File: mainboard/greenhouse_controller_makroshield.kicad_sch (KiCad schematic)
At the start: 39 parts

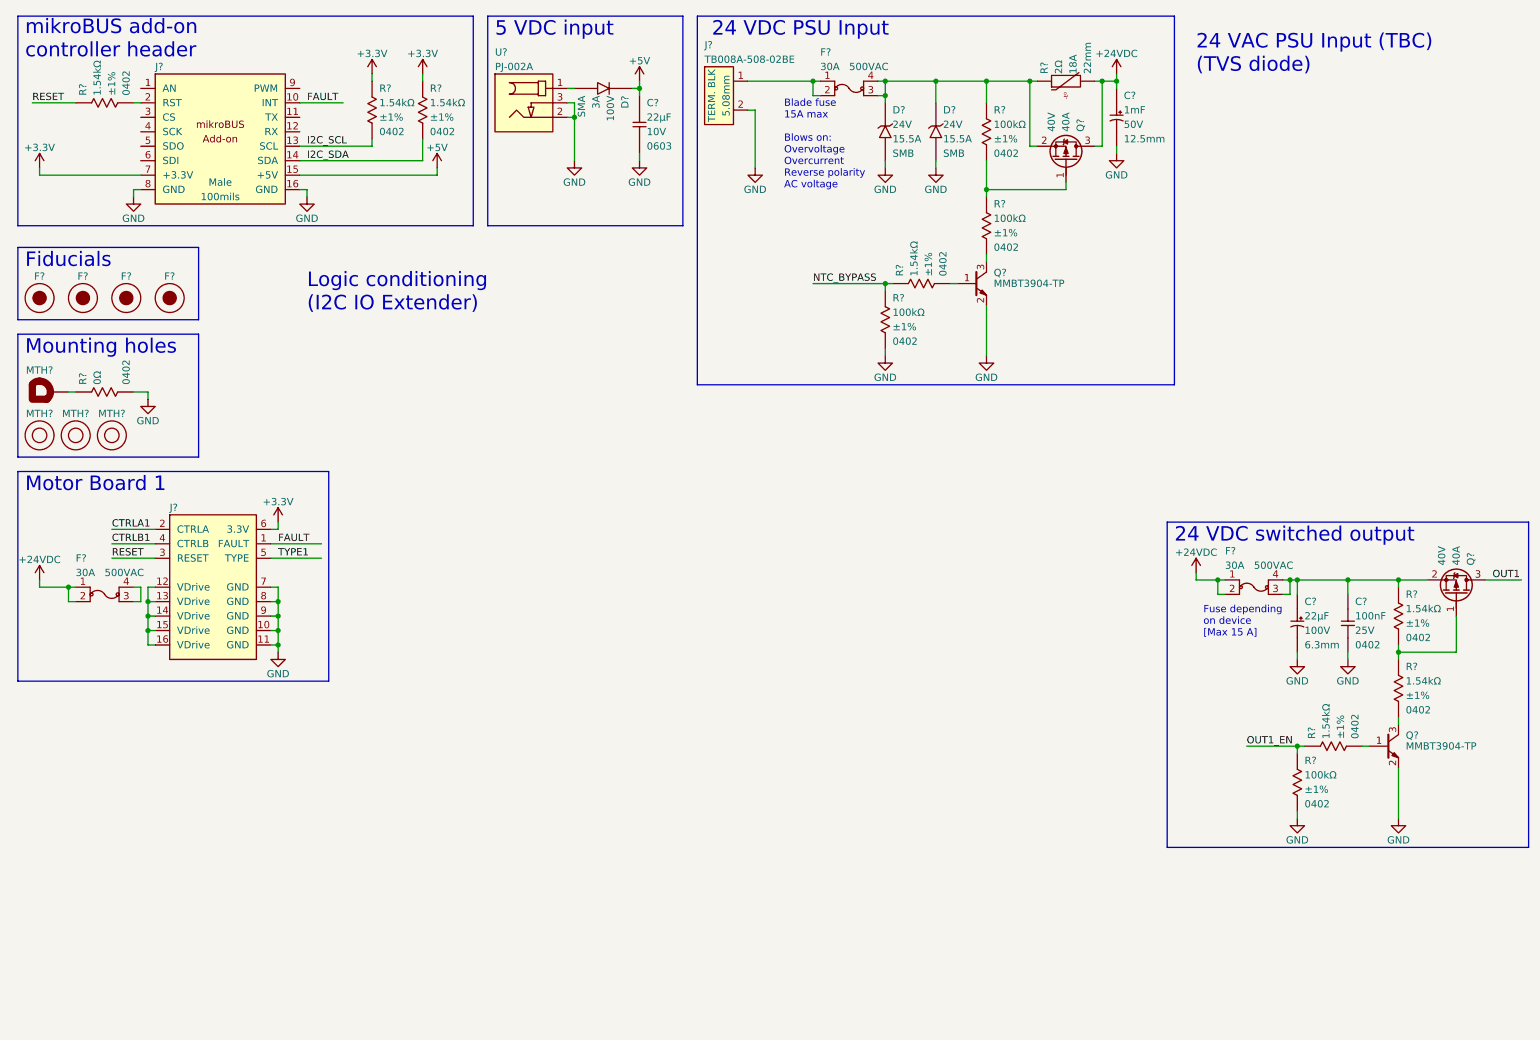
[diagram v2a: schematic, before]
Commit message: Add IO expanders, add simple PMOS switch, add 5V TVS,
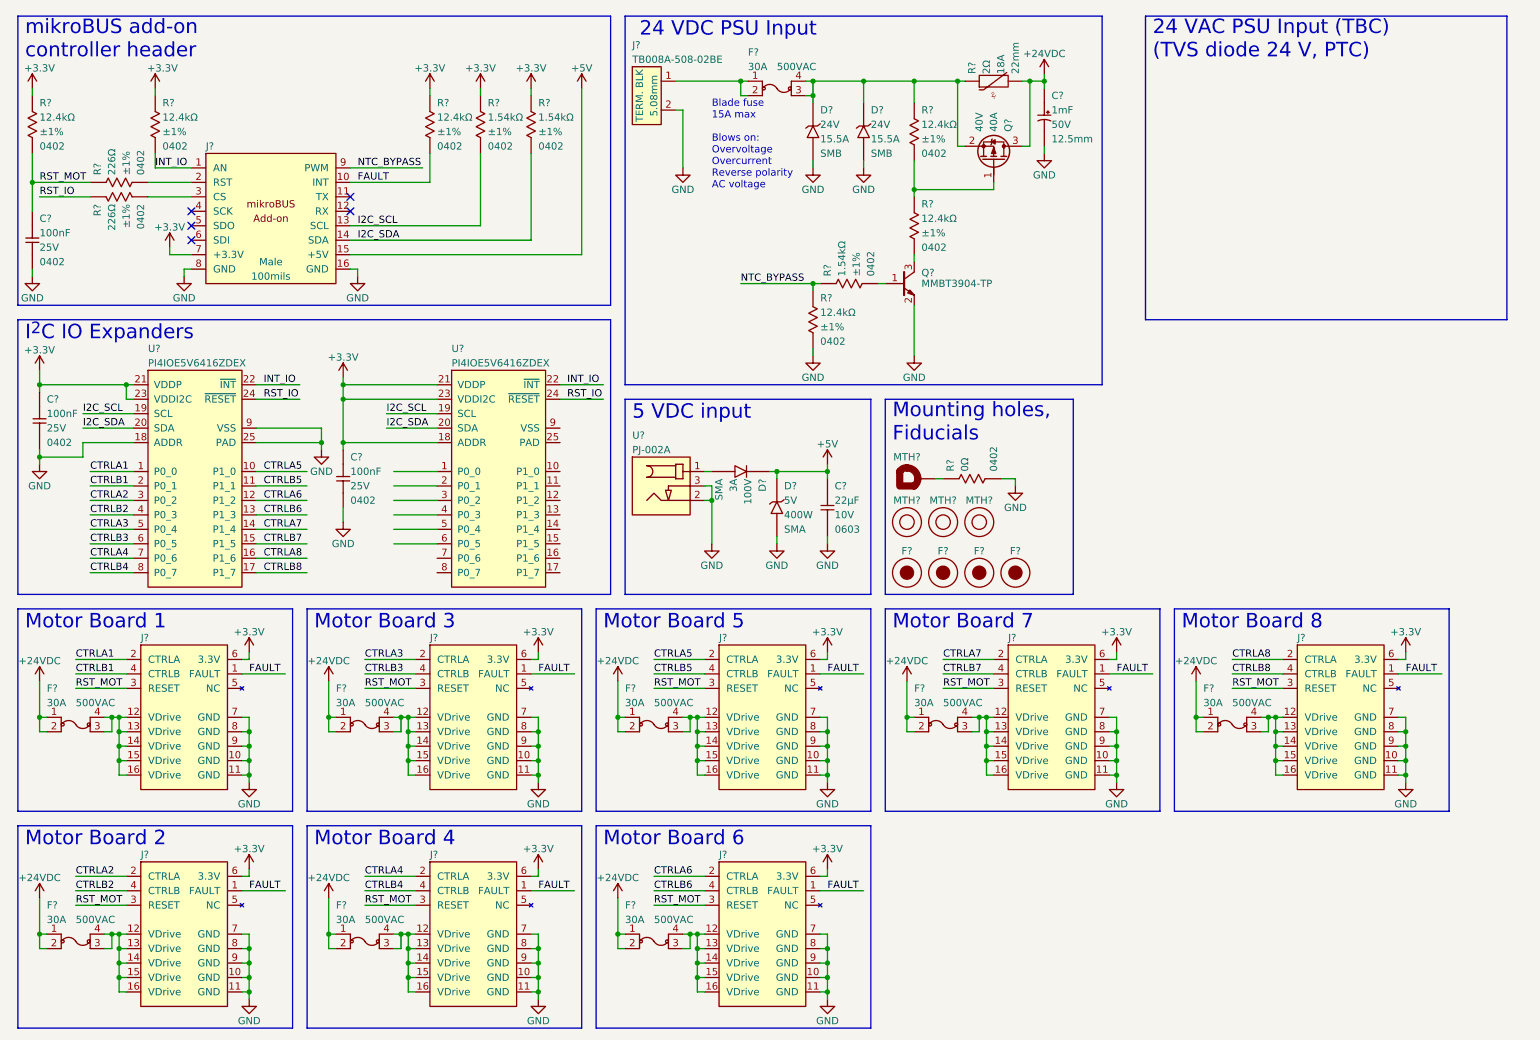
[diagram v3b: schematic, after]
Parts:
- removed C?: CAP_CER_100NF_25V_0402, connaxio-capacitors:CAP_CER_0402_1005M, symbol connaxio-capacitors:CAP_CER_100NF_25V_0402
- removed C?: CAP_AE_22UF_100V_TH_6.3MM, connaxio-capacitors:CAP_AE_RAD_D6.3_H12.5_P2.5, symbol connaxio-capacitors:CAP_AE_22UF_100V_TH_6.3MM
- removed F?: FUS_BLADE_3522, connaxio-connectors:FUS_BLADE_3522, symbol connaxio-connectors:FUS_BLADE_3522
- removed Q?: TRX_PMOS_AOD4189, connaxio-sop:TO-252-3, symbol connaxio-transistors:TRX_PMOS_AOD4189
- removed Q?: TRX_NPN_MMBT3904-TP, connaxio-sop:SOT-23-3, symbol connaxio-transistors:TRX_NPN_MMBT3904-TP
- removed R? (x4): RES_100KΩ_1%_0402, connaxio-resistors:RES_0402_1005M, symbol connaxio-resistors:RES_100KΩ_1%_0402
- removed R? (x4): RES_1.54KΩ_1%_0402, connaxio-resistors:RES_0402_1005M, symbol connaxio-resistors:RES_1.54KΩ_1%_0402
- added C? (x3): CAP_CER_100NF_25V_0402, connaxio-capacitors:CAP_CER_0402_1005M, symbol connaxio-capacitors:CAP_CER_100NF_25V_0402
- added D?: DIO_TVS_5V_UNI_SMA, connaxio-diodes:DO-214AC_SMA, symbol connaxio-diodes:DIO_TVS_5V_UNI_SMA
- added F? (x7): FUS_BLADE_3522, connaxio-connectors:FUS_BLADE_3522, symbol connaxio-connectors:FUS_BLADE_3522
- added J? (x7): CON_CONNAXIO_MOTOR_DRIVER, connaxio-connectors:CON_HDR_100MILS_F_TH_2X8, symbol connaxio-connectors:CON_CONNAXIO_MOTOR_DRIVER
- added R? (x6): RES_12.4KΩ_1%_0402, connaxio-resistors:RES_0402_1005M, symbol connaxio-resistors:RES_12.4KΩ_1%_0402
- added R? (x2): RES_226Ω_1%_0402, connaxio-resistors:RES_0402_1005M, symbol connaxio-resistors:RES_226Ω_1%_0402
- added U? (x2): IO_EXP_PI4IOE5V6416ZDEX, connaxio-fp:QFN-24_4x4_P0.5_EP2.7X2.7, symbol connaxio-ic:IO_EXP_PI4IOE5V6416ZDEX
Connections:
- net +24VDC: now also F?.1, F?.1, F?.1, F?.1, F?.1, F?.1, F?.1, F?.2, F?.2, F?.2, F?.2, F?.2, F?.2, F?.2
- net +3.3V: now also C?.1, C?.1, J?.6 (3.3V), J?.6 (3.3V), J?.6 (3.3V), J?.6 (3.3V), J?.6 (3.3V), J?.6 (3.3V), J?.6 (3.3V), R?.1, R?.1, R?.1, U?.18 (ADDR), U?.21 (VDDP), U?.21 (VDDP), U?.23 (VDDI2C), U?.23 (VDDI2C)
- net +5V: now also D?.1 (K)
- net CTRLA1: now also U?.1 (P0_0)
- net CTRLB1: now also U?.2 (P0_1)
- net FAULT: now also J?.1 (FAULT), J?.1 (FAULT), J?.1 (FAULT), J?.1 (FAULT), J?.1 (FAULT), J?.1 (FAULT), J?.1 (FAULT), R?.2
- net GND: now also C?.2, C?.2, C?.2, D?.2 (A), J?.10 (GND), J?.10 (GND), J?.10 (GND), J?.10 (GND), J?.10 (GND), J?.10 (GND), J?.10 (GND), J?.11 (GND), J?.11 (GND), J?.11 (GND), J?.11 (GND), J?.11 (GND), J?.11 (GND), J?.11 (GND), J?.7 (GND), J?.7 (GND), J?.7 (GND), J?.7 (GND), J?.7 (GND), J?.7 (GND), J?.7 (GND), J?.8 (GND), J?.8 (GND), J?.8 (GND), J?.8 (GND), J?.8 (GND), J?.8 (GND), J?.8 (GND), J?.9 (GND), J?.9 (GND), J?.9 (GND), J?.9 (GND), J?.9 (GND), J?.9 (GND), J?.9 (GND), R?.2, U?.18 (ADDR), U?.25 (PAD), U?.9 (VSS)
- net I2C_SCL: now also U?.19 (SCL), U?.19 (SCL)
- net I2C_SDA: now also U?.20 (SDA), U?.20 (SDA)
- net NTC_BYPASS: now also J?.9 (PWM), R?.1
- net at D?.1 (K), D?.1 (K), F?.3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: now also R?.1
- net at Q?.1 (G): now also R?.1, R?.2
- net at Q?.3 (C): now also R?.2
- net at J?.2 (RST): now also R?.2
- net at F?.3, F?.4: now also J?.12 (VDrive), J?.13 (VDrive), J?.14 (VDrive), J?.15 (VDrive), J?.16 (VDrive)
- net INT_IO: now reaches J?.1 (AN)
- net INT_IO: now also R?.2, U?.22 (~{INT}), U?.22 (~{INT})
- net at J?.3 (CS): now also R?.2
- net RESET renamed RST_MOT
- net RST_MOT: now also C?.1, J?.3 (RESET), J?.3 (RESET), J?.3 (RESET), J?.3 (RESET), J?.3 (RESET), J?.3 (RESET), J?.3 (RESET), R?.1, R?.2
- net TYPE1: no longer names the net of J?.5 (NC)
- new net: F?.3, F?.4, J?.12 (VDrive), J?.13 (VDrive), J?.14 (VDrive), J?.15 (VDrive), J?.16 (VDrive) (x7)
- new net CTRLA2: J?.2 (CTRLA), U?.3 (P0_2)
- new net CTRLA3: J?.2 (CTRLA), U?.5 (P0_4)
- new net CTRLA4: J?.2 (CTRLA), U?.7 (P0_6)
- new net CTRLA5: J?.2 (CTRLA), U?.10 (P1_0)
- new net CTRLA6: J?.2 (CTRLA), U?.12 (P1_2)
- new net CTRLA7: J?.2 (CTRLA), U?.14 (P1_4)
- new net CTRLA8: J?.2 (CTRLA), U?.16 (P1_6)
- new net CTRLB2: J?.4 (CTRLB), U?.4 (P0_3)
- new net CTRLB3: J?.4 (CTRLB), U?.6 (P0_5)
- new net CTRLB4: J?.4 (CTRLB), U?.8 (P0_7)
- new net CTRLB5: J?.4 (CTRLB), U?.11 (P1_1)
- new net CTRLB6: J?.4 (CTRLB), U?.13 (P1_3)
- new net CTRLB7: J?.4 (CTRLB), U?.15 (P1_5)
- new net CTRLB8: J?.4 (CTRLB), U?.17 (P1_7)
- new net RST_IO: R?.1, U?.24 (~{RESET}), U?.24 (~{RESET})
- no-connect marks 0 -> 5
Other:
- note added: "24 VAC PSU Input (TBC) (TVS diode 24 V, PTC)"
- note added: "I^{2}C IO Expanders"
- note added: "Motor Board 2"
- note added: "Motor Board 3"
- note added: "Motor Board 4"
- note added: "Motor Board 5"
- note added: "Motor Board 6"
- note added: "Motor Board 7"
- note added: "Motor Board 8"
- note added: "Mounting holes, Fiducials"
- note removed: "24 VAC PSU Input (TBC) (TVS diode)"
- note removed: "24 VDC switched output"
- note removed: "Fiducials"
- note removed: "Fuse depending on device [Max 15 A]"
- note removed: "Logic conditioning (I2C IO Extender)"
- note removed: "Mounting holes"
- moved on the sheet: C?, D?, F?, J?, MTH?, Q?, R?, U?

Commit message: Add motor driver page and I2C proteciton adapter, current & temp sensor
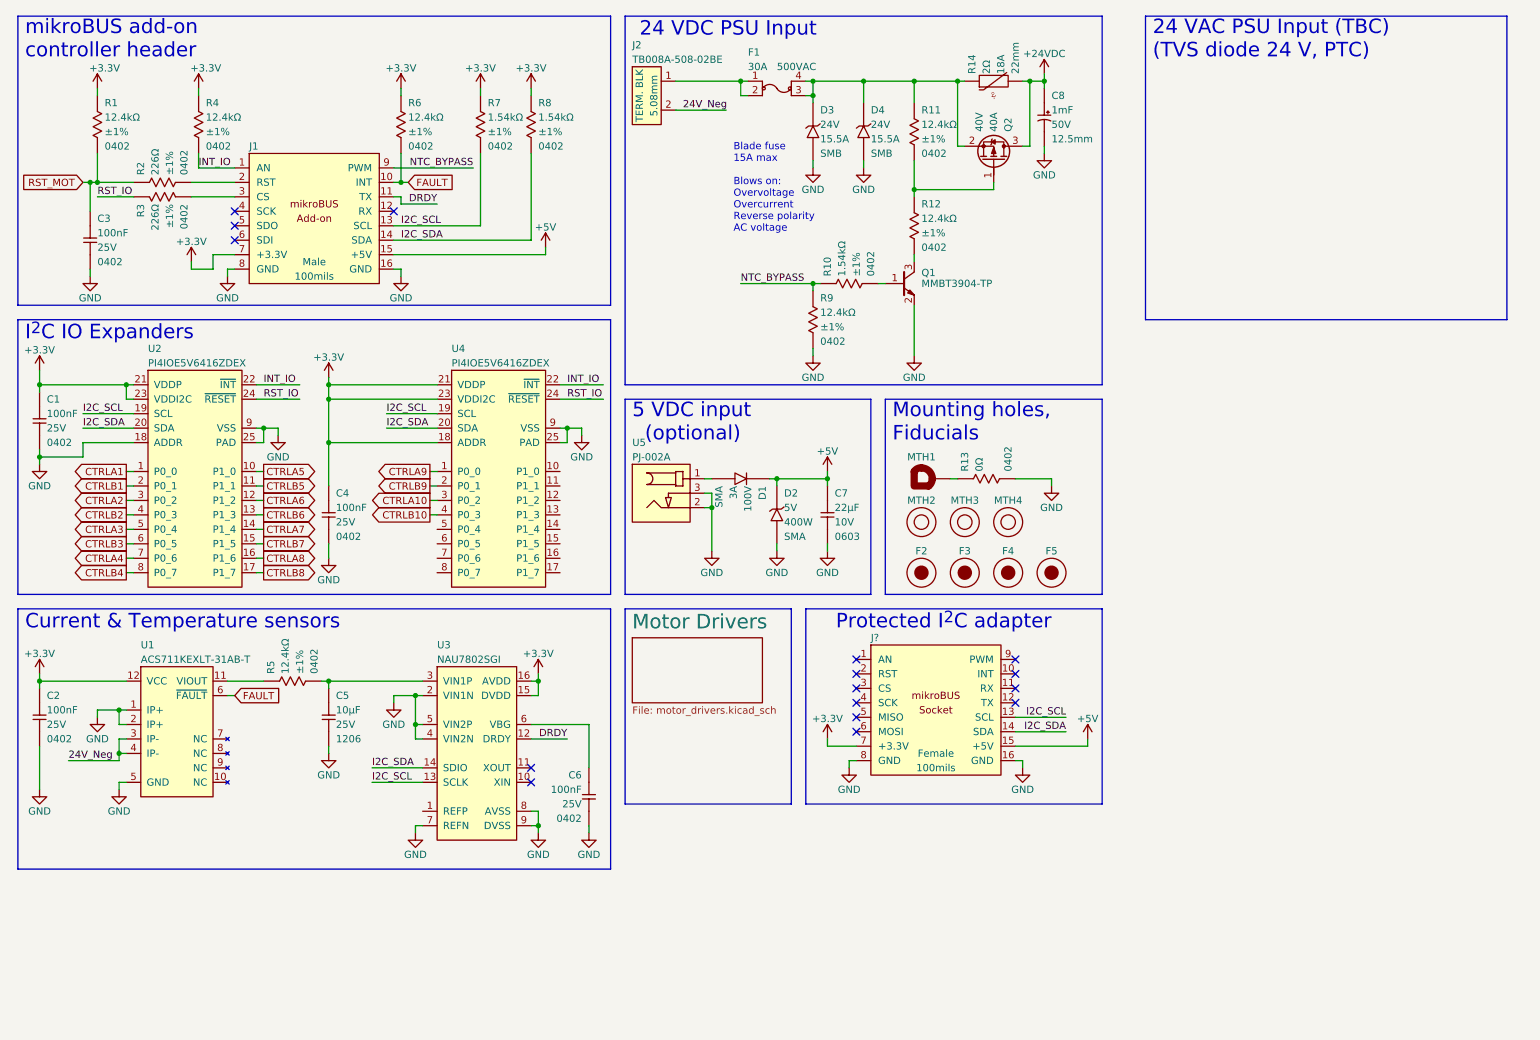
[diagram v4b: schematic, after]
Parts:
- removed F? (x8): FUS_BLADE_3522, connaxio-connectors:FUS_BLADE_3522, symbol connaxio-connectors:FUS_BLADE_3522
- removed J? (x8): CON_CONNAXIO_MOTOR_DRIVER, connaxio-connectors:CON_HDR_100MILS_F_TH_2X8, symbol connaxio-connectors:CON_CONNAXIO_MOTOR_DRIVER
- added C2, C6: CAP_CER_100NF_25V_0402, connaxio-capacitors:CAP_CER_0402_1005M, symbol connaxio-capacitors:CAP_CER_100NF_25V_0402
- added C5: CAP_CER_10UF_25V_1206, connaxio-capacitors:CAP_CER_1206_3216M, symbol connaxio-capacitors:CAP_CER_10UF_25V_1206
- added J?: CON_HDR_MIKROBUS_SOCKET_TH, connaxio-connectors:CON_HDR_MIKROBUS_SOCKET_TH, symbol connaxio-connectors:CON_HDR_MIKROBUS_SOCKET_TH
- added R5: RES_12.4KΩ_1%_0402, connaxio-resistors:RES_0402_1005M, symbol connaxio-resistors:RES_12.4KΩ_1%_0402
- added U1: SUN_CUR_ACS711KEXLT-31AB-T, connaxio-fp:QFN-12_CUR_SEN_ACS7, symbol connaxio-ic:SUN_CUR_ACS711KEXLT-31AB-T
- added U3: ADC_NAU7802SGI, connaxio-sop:SOIC-16_3.9X9.9_P1.27, symbol connaxio-ic:ADC_NAU7802SGI
- gave numbers to parts that had none: 38
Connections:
- net +3.3V: now also C2.1, J?.7 (+3.3V), U1.12 (VCC), U3.15 (DVDD), U3.16 (AVDD)
- net +5V: now also J?.15 (+5V)
- net FAULT: now also U1.6 (~{FAULT})
- net GND: now also U4.25 (PAD), U4.9 (VSS), C2.2, C5.2, C6.2, J?.16 (GND), J?.8 (GND), U1.1 (IP+), U1.2 (IP+), U1.5 (GND), U3.2 (VIN1N), U3.4 (VIN2N), U3.5 (VIN2P), U3.7 (REFN), U3.8 (AVSS), U3.9 (DVSS); no longer J2.2
- net I2C_SCL: now also J?.13 (SCL), U3.13 (SCLK)
- net I2C_SDA: now also J?.14 (SDA), U3.14 (SDIO)
- net CTRLA9: now reaches U4.1 (P0_0)
- net CTRLB9: now reaches U4.2 (P0_1)
- net CTRLA10: now reaches U4.3 (P0_2)
- net CTRLB10: now reaches U4.4 (P0_3)
- net DRDY: now reaches J1.11 (TX)
- net DRDY: now also U3.12 (DRDY)
- new net: C5.1, R5.2, U3.3 (VIN1P)
- new net: R5.1, U1.11 (VIOUT)
- new net: C6.1, U3.6 (VBG)
- new net 24V_Neg: J2.2, U1.3 (IP-), U1.4 (IP-)
- no-connect marks 5 -> 16
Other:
- added sheet Motor Drivers (motor_drivers.kicad_sch)
- note added: "5 VDC input (optional)"
- note added: "Current & Temperature sensors"
- note added: "Protected I^{2}C adapter"
- note removed: "5 VDC input"
- note removed: "Motor Board 1"
- note removed: "Motor Board 2"
- note removed: "Motor Board 3"
- note removed: "Motor Board 4"
- note removed: "Motor Board 5"
- note removed: "Motor Board 6"
- note removed: "Motor Board 7"
- note removed: "Motor Board 8"
- moved on the sheet: C3, C4, C7, D1, D2, F2, F3, F4, F5, J1, MTH1, MTH2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

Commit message: Move fuse to motor driver board Optimize board array schematic (hierarchical schematics)
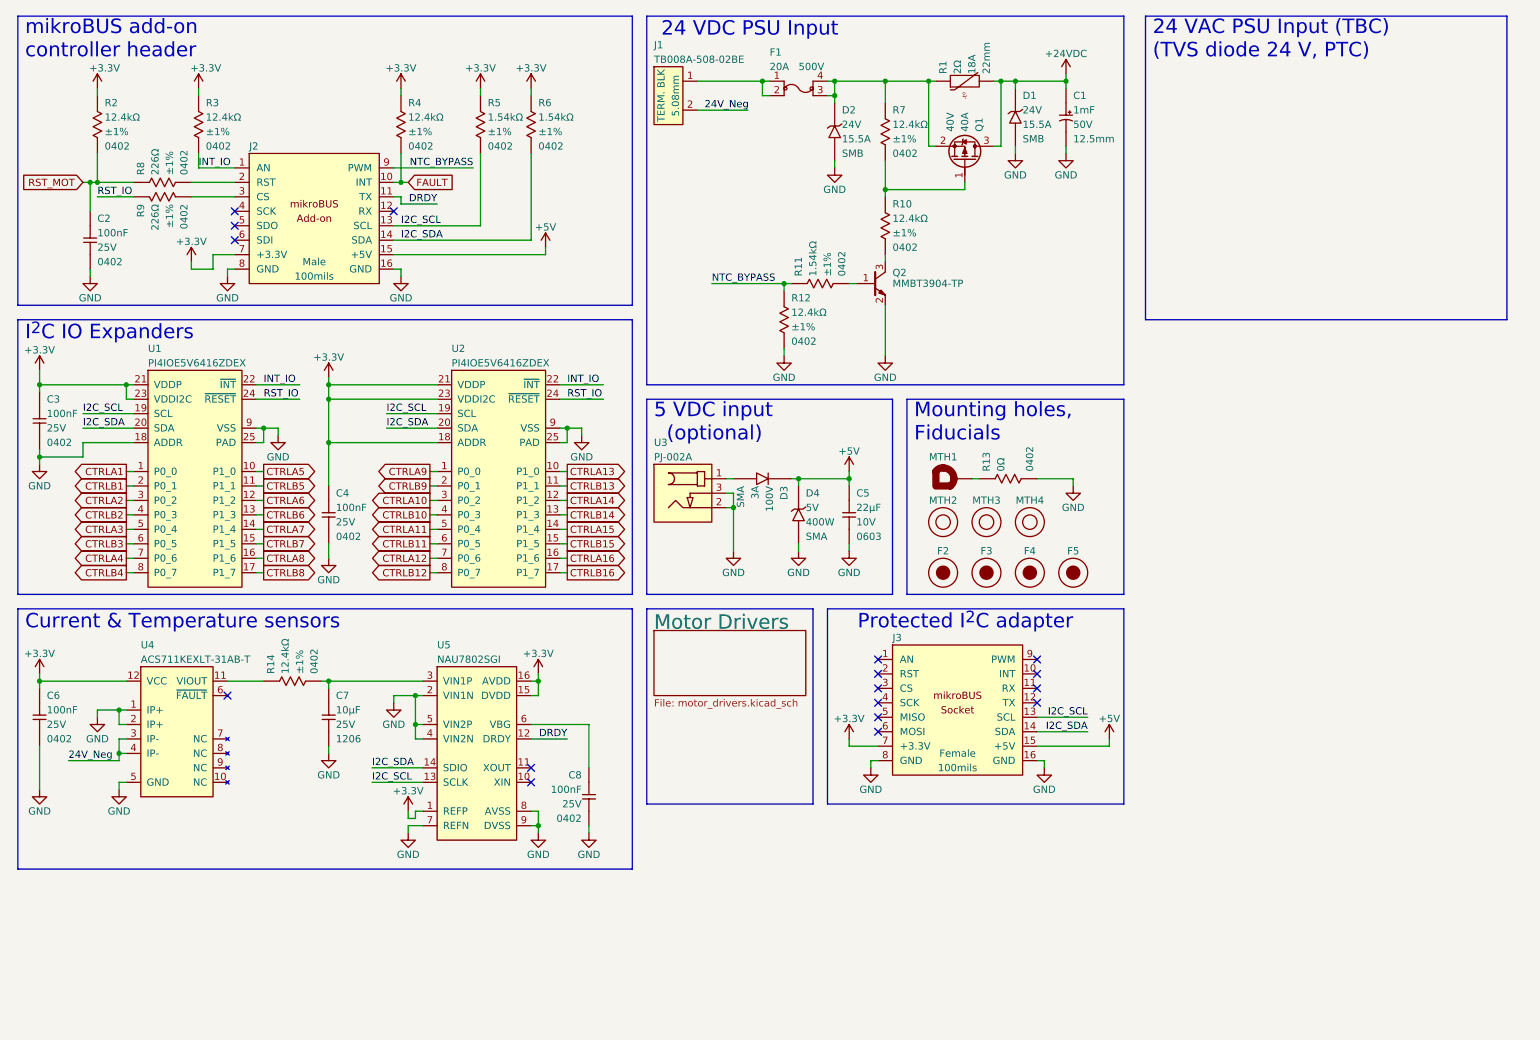
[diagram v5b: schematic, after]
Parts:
- removed D4: DIO_TVS_24V_UNI_SMB, connaxio-diodes:DO-124AA_SMB, symbol connaxio-diodes:DIO_TVS_24V_UNI_SMB
- removed F1: FUS_BLADE_3522, connaxio-connectors:FUS_BLADE_3522, symbol connaxio-connectors:FUS_BLADE_3522
- added D1: DIO_TVS_24V_UNI_SMB, connaxio-diodes:DO-124AA_SMB, symbol connaxio-diodes:DIO_TVS_24V_UNI_SMB
- added F1: FUS_BLADE_MINI_3588-1, connaxio-connectors:FUS_BLADE_MINI_3588-1, symbol connaxio-connectors:FUS_BLADE_MINI_3588-1
- gave numbers to parts that had none: 1
- renumbered C8 to C1, C3 to C2, C1 to C3, C7 to C5, C2 to C6, C5 to C7, C6 to C8, D3 to D2, D1 to D3, D2 to D4, J2 to J1, J1 to J2, Q2 to Q1, Q1 to Q2, R14 to R1, R12 to R10, R10 to R11, R9 to R12, R5 to R14, R1 to R2, R4 to R3, R6 to R4, R7 to R5, R8 to R6, R11 to R7, R2 to R8, R3 to R9, U2 to U1, U4 to U2, U5 to U3, U1 to U4, U3 to U5
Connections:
- net +24VDC: now also D1.1 (K)
- net +3.3V: now also U5.1 (REFP)
- net FAULT: no longer U4.6 (~{FAULT})
- net GND: now also D1.2 (A)
- net at D2.1 (K), Q1.2 (S), R1.1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: now also F1.3, F1.4
- net CTRLA13: now reaches U2.10 (P1_0)
- net CTRLB13: now reaches U2.11 (P1_1)
- net CTRLA14: now reaches U2.12 (P1_2)
- net CTRLB14: now reaches U2.13 (P1_3)
- net CTRLA15: now reaches U2.14 (P1_4)
- net CTRLB15: now reaches U2.15 (P1_5)
- net CTRLA16: now reaches U2.16 (P1_6)
- net CTRLB16: now reaches U2.17 (P1_7)
- net CTRLA11: now reaches U2.5 (P0_4)
- net CTRLB11: now reaches U2.6 (P0_5)
- net CTRLA12: now reaches U2.7 (P0_6)
- net CTRLB12: now reaches U2.8 (P0_7)
- net at J1.1: now also F1.1, F1.2
- no-connect marks 16 -> 17
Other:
- note removed: "Blade fuse 15A max Blows on: Overvoltage Overcurrent Reverse polarity AC voltage"
- moved on the sheet: C1, C5, D2, D3, D4, F2, F3, F4, F5, J1, J3, MTH1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
